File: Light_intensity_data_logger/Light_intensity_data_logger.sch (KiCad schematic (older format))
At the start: 15 parts

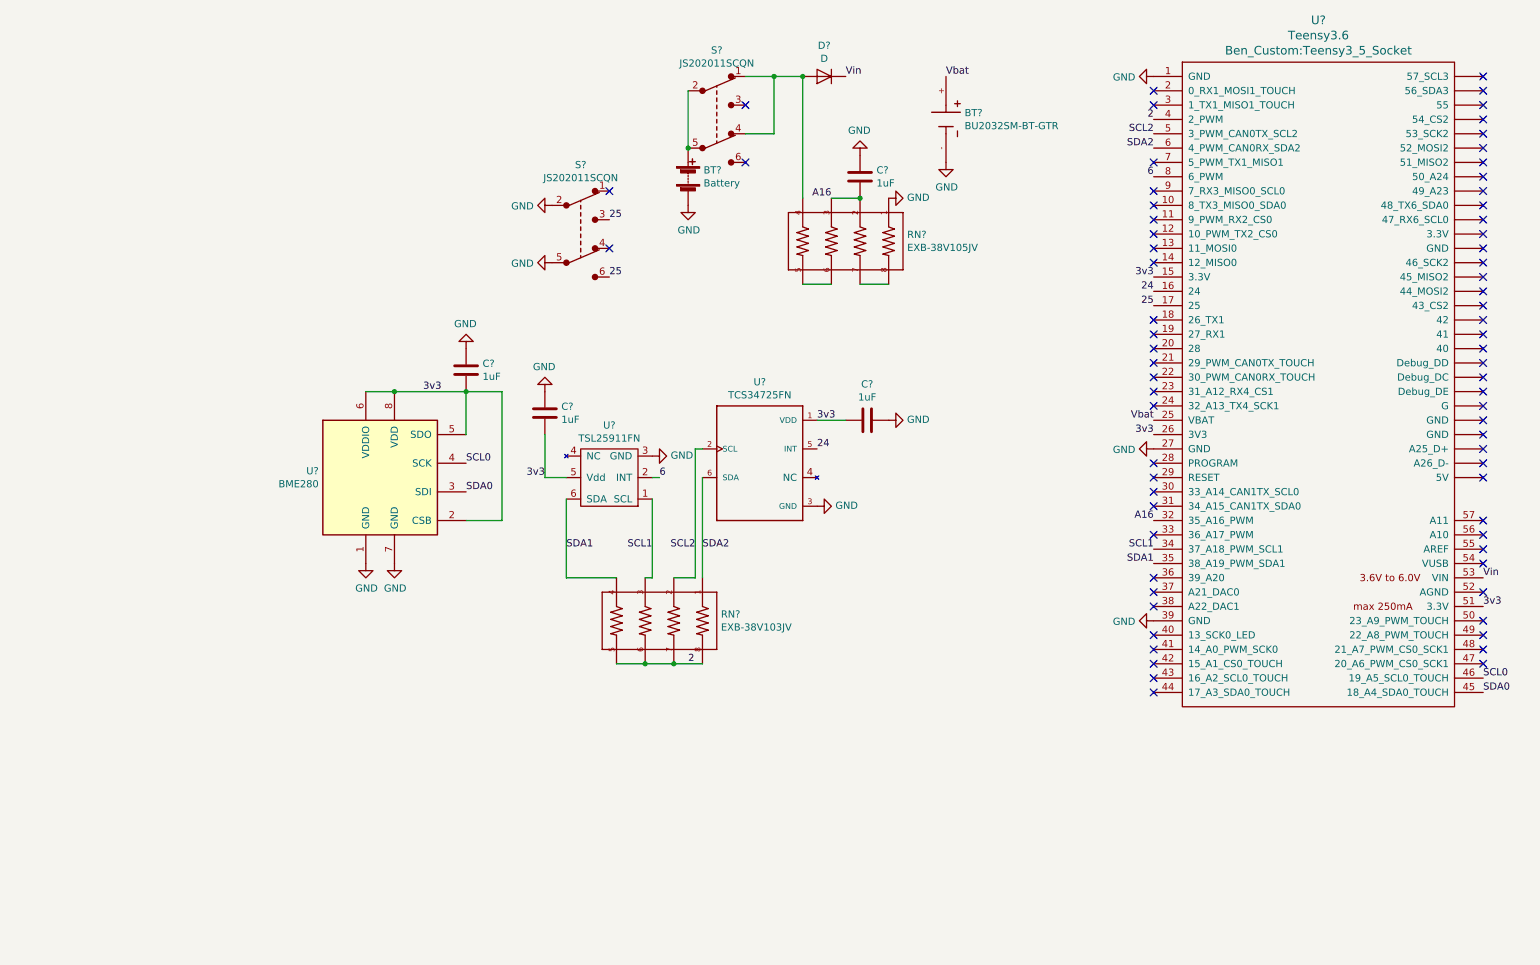
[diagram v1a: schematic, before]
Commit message: Add joystick and display
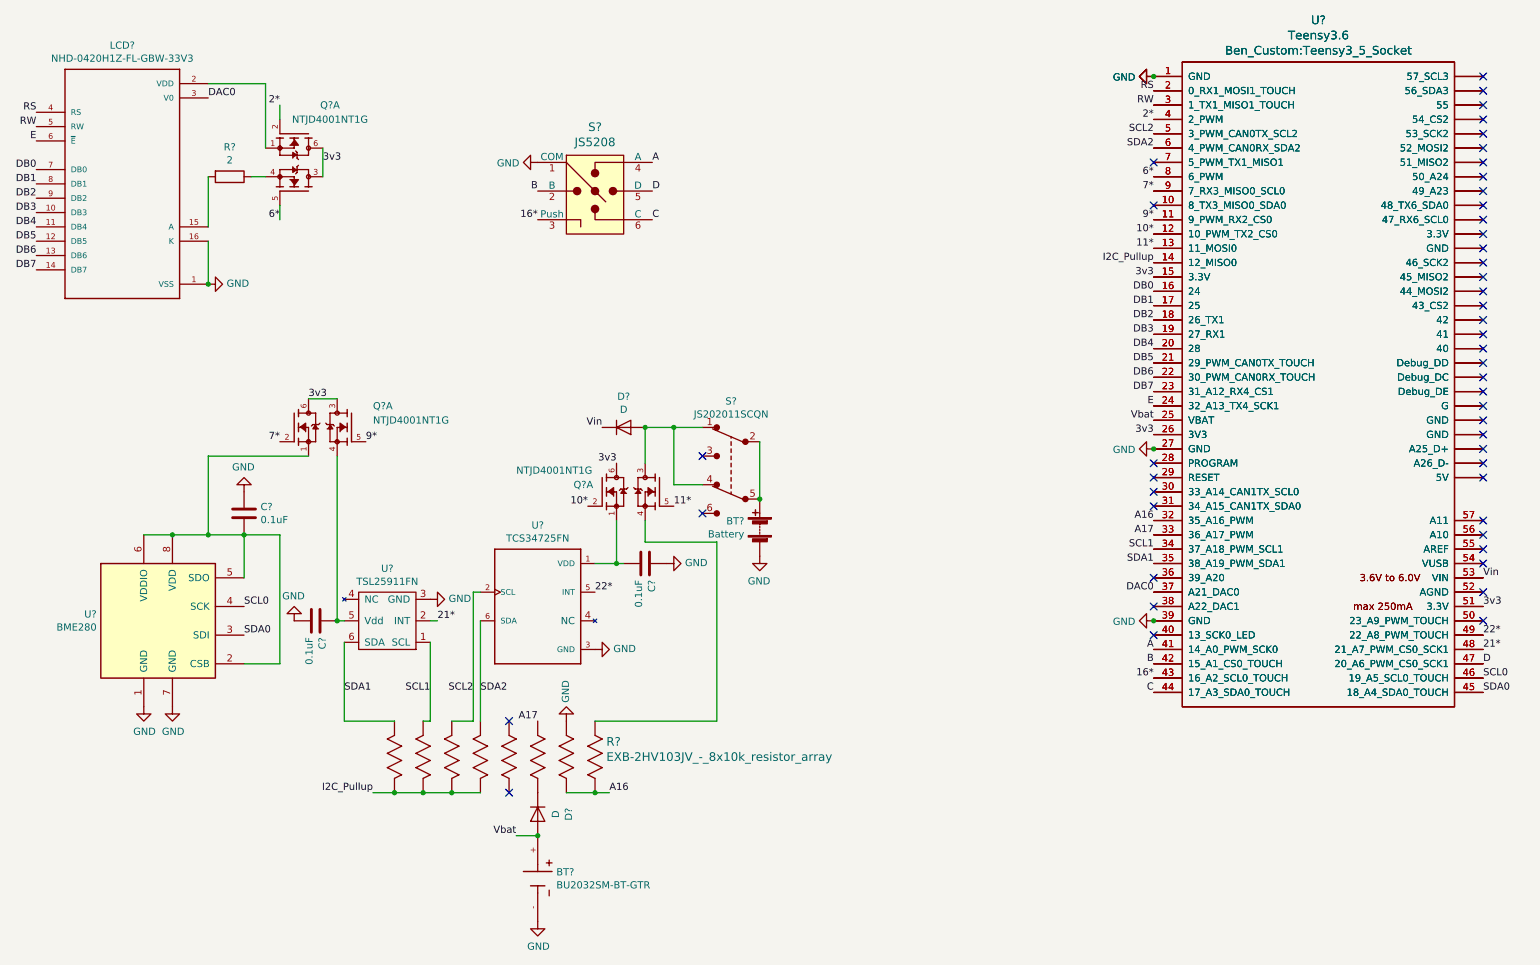
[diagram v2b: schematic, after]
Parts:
- removed C? (x3): 1uF, Capacitors_SMD:C_0603, symbol device:C
- removed RN?: EXB-38V103JV, RESCAXS80P320X160X60-8N, symbol Ben_custom:EXB-38V103JV
- removed RN?: EXB-38V105JV, RESCAXS80P320X160X60-8N, symbol Ben_custom:EXB-38V103JV
- removed S?: JS202011SCQN, digikey-footprints:Switch_Slide_JS202011SCQN, symbol dk_Slide-Switches:JS202011SCQN
- added C? (x2): 0.1uF, Capacitors_SMD:C_0603, symbol device:C
- added D?: D, Diodes_SMD:D_SOD-323, symbol device:D
- added LCD?: NHD-0420H1Z-FL-GBW-33V3, LCD_NHD-0420H1Z-FL-GBW-33V3, symbol Ben_custom:NHD-0420H1Z-FL-GBW-33V3
- added Q? (x3): NTJD4001NT1G, TO_SOT_Packages_SMD:SOT-363_SC-70-6, symbol Ben_custom:NTJD4001NT1G
- added R?: EXB-2HV103JV_-_8x10k_resistor_array, Ben_Custom:Resistor_array_1506_8x, symbol Ben_custom:EXB-2HV103JV_-_8x10k_resistor_array
- added R?: 2, Resistors_SMD:R_0603, symbol device:R
- added S?: JS5208, digikey-footprints:Switch_Nav_12.4x12.4mm_SMD_JS5208, symbol dk_Navigation-Switches-Joystick:JS5208
- added U?: Teensy3.6, Ben_Custom:Teensy3_5_Socket, symbol teensy:Teensy3.6
- C?: value 1uF -> 0.1uF; Part# 1276-6524-1-ND -> 311-1344-1-ND
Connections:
- net 3v3: now also Q?.3 (D2), Q?.3 (D2), Q?.6 (D1), Q?.6 (D1), Q?.6 (D1), U?.15 (3.3V), U?.26 (3V3), U?.51 (3.3V); no longer C?.2, U?.1 (VDD), U?.2 (CSB), U?.5 (SDO), U?.5 (Vdd), U?.6 (VDDIO), U?.8 (VDD)
- net A16: now also R?.15, R?.16, U?.32 (35_A16_PWM)
- net GND: now also C?.1, C?.2, LCD?.1 (VSS), LCD?.16 (K), R?.2, S?.1 (COM), U?.1 (GND), U?.27 (GND), U?.39 (GND)
- net SCL0: now also U?.46 (19_A5_SCL0_TOUCH)
- net SCL1: now also R?.7, U?.34 (37_A18_PWM_SCL1)
- net SCL2: now also R?.6, U?.5 (3_PWM_CAN0TX_SCL2)
- net SDA0: now also U?.45 (18_A4_SDA0_TOUCH)
- net SDA1: now also R?.8, U?.35 (38_A19_PWM_SDA1)
- net SDA2: now also R?.5, U?.6 (4_PWM_CAN0RX_SDA2)
- net Vbat: now also D?.2 (A), U?.25 (VBAT)
- net Vin: now also U?.53 (VIN)
- net at U?.10 (8_TX3_MISO0_SDA0): now also U?.10 (8_TX3_MISO0_SDA0)
- net 9*: now reaches U?.11 (9_PWM_RX2_CS0)
- net 9*: now also Q?.5 (G2), U?.11 (9_PWM_RX2_CS0)
- net 10*: now reaches U?.12 (10_PWM_TX2_CS0)
- net 10*: now also Q?.2 (G1), U?.12 (10_PWM_TX2_CS0)
- net 11*: now reaches U?.13 (11_MOSI0)
- net 11*: now also Q?.5 (G2), U?.13 (11_MOSI0)
- net I2C_Pullup: now reaches U?.14 (12_MISO0)
- net I2C_Pullup: now also R?.10, R?.11, R?.12, R?.9, U?.14 (12_MISO0)
- net DB2: now reaches U?.18 (26_TX1)
- net DB2: now also LCD?.9 (DB2), U?.18 (26_TX1)
- net DB3: now reaches U?.19 (27_RX1)
- net DB3: now also LCD?.10 (DB3), U?.19 (27_RX1)
- net RS: now reaches U?.2 (0_RX1_MOSI1_TOUCH)
- net RS: now also LCD?.4 (RS), U?.2 (0_RX1_MOSI1_TOUCH)
- net DB4: now reaches U?.20 (28)
- net DB4: now also LCD?.11 (DB4), U?.20 (28)
- net DB5: now reaches U?.21 (29_PWM_CAN0TX_TOUCH)
- net DB5: now also LCD?.12 (DB5), U?.21 (29_PWM_CAN0TX_TOUCH)
- net DB6: now reaches U?.22 (30_PWM_CAN0RX_TOUCH)
- net DB6: now also LCD?.13 (DB6), U?.22 (30_PWM_CAN0RX_TOUCH)
- net DB7: now reaches U?.23 (31_A12_RX4_CS1)
- net DB7: now also LCD?.14 (DB7), U?.23 (31_A12_RX4_CS1)
- net E: now reaches U?.24 (32_A13_TX4_SCK1)
- net E: now also LCD?.6 (~E~), U?.24 (32_A13_TX4_SCK1)
- net at U?.28 (PROGRAM): now also U?.28 (PROGRAM)
- net at U?.29 (RESET): now also U?.29 (RESET)
- net RW: now reaches U?.3 (1_TX1_MISO1_TOUCH)
- net RW: now also LCD?.5 (RW), U?.3 (1_TX1_MISO1_TOUCH)
- net at U?.30 (33_A14_CAN1TX_SCL0): now also U?.30 (33_A14_CAN1TX_SCL0)
- net at U?.31 (34_A15_CAN1TX_SDA0): now also U?.31 (34_A15_CAN1TX_SDA0)
- net A17: now reaches U?.33 (36_A17_PWM)
- net A17: now also R?.3, U?.33 (36_A17_PWM)
- net at U?.36 (39_A20): now also U?.36 (39_A20)
- net DAC0: now reaches U?.37 (A21_DAC0)
- net DAC0: now also LCD?.3 (V0), U?.37 (A21_DAC0)
- net at U?.38 (A22_DAC1): now also U?.38 (A22_DAC1)
- net at U?.40 (13_SCK0_LED): now also U?.40 (13_SCK0_LED)
- net A: now reaches U?.41 (14_A0_PWM_SCK0)
- net A: now also S?.4 (A), U?.41 (14_A0_PWM_SCK0)
- net B: now reaches U?.42 (15_A1_CS0_TOUCH)
- net B: now also S?.2 (B), U?.42 (15_A1_CS0_TOUCH)
- net 16*: now reaches U?.43 (16_A2_SCL0_TOUCH)
- net 16*: now also S?.3 (Push), U?.43 (16_A2_SCL0_TOUCH)
- net C: now reaches U?.44 (17_A3_SDA0_TOUCH)
- net C: now also S?.6 (C), U?.44 (17_A3_SDA0_TOUCH)
- net D: now reaches U?.47 (20_A6_PWM_CS0_SCK1)
- net D: now also S?.5 (D), U?.47 (20_A6_PWM_CS0_SCK1)
- net 21*: now reaches U?.48 (21_A7_PWM_CS0_SCK1)
- net 21*: now also U?.2 (INT), U?.48 (21_A7_PWM_CS0_SCK1)
- net 22*: now reaches U?.49 (22_A8_PWM_TOUCH)
- net 22*: now also U?.5 (INT), U?.49 (22_A8_PWM_TOUCH)
- net at U?.50 (23_A9_PWM_TOUCH): now also U?.50 (23_A9_PWM_TOUCH)
- net at U?.52 (AGND): now also U?.52 (AGND)
- net at U?.54 (VUSB): now also U?.54 (VUSB)
- net at U?.55 (AREF): now also U?.55 (AREF)
- net at U?.56 (A10): now also U?.56 (A10)
- net at U?.57 (A11): now also U?.57 (A11)
- net at U?.7 (5_PWM_TX1_MISO1): now also U?.7 (5_PWM_TX1_MISO1)
- net 7*: now reaches U?.9 (7_RX3_MISO0_SCL0)
- net 7*: now also Q?.2 (G1), U?.9 (7_RX3_MISO0_SCL0)
- net at U?.~ (GND): now also U?.~ (GND)
- net at D?.2 (A), S?.1, S?.4: now also Q?.3 (D2)
- net 2 renamed 2*
- net 2*: now also Q?.2 (G1), U?.4 (2_PWM)
- net 24 renamed DB0
- net DB0: now also LCD?.7 (DB0), U?.16 (24); no longer U?.5 (INT)
- net 25 renamed DB1
- net DB1: now also LCD?.8 (DB1), U?.17 (25)
- net 6 renamed 6*
- net 6*: now also Q?.5 (G2), U?.8 (6_PWM); no longer U?.2 (INT)
- new net: U?.~ (GND), U?.~ (GND) (x28)
- new net: C?.2, Q?.1 (S1), U?.1 (VDD)
- new net: C?.1, Q?.4 (S2), U?.5 (Vdd)
- new net: C?.2, Q?.1 (S1), U?.2 (CSB), U?.5 (SDO), U?.6 (VDDIO), U?.8 (VDD)
- new net: LCD?.15 (A), R?.2
- new net: LCD?.2 (VDD), Q?.1 (S1)
- new net: Q?.4 (S2), R?.1 (x2)
- new net: D?.1 (K), R?.14
- no-connect marks 71 -> 48
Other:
- moved on the sheet: BT?, C?, D?, S?, U?

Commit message: Add claw headers and initial PCB layout
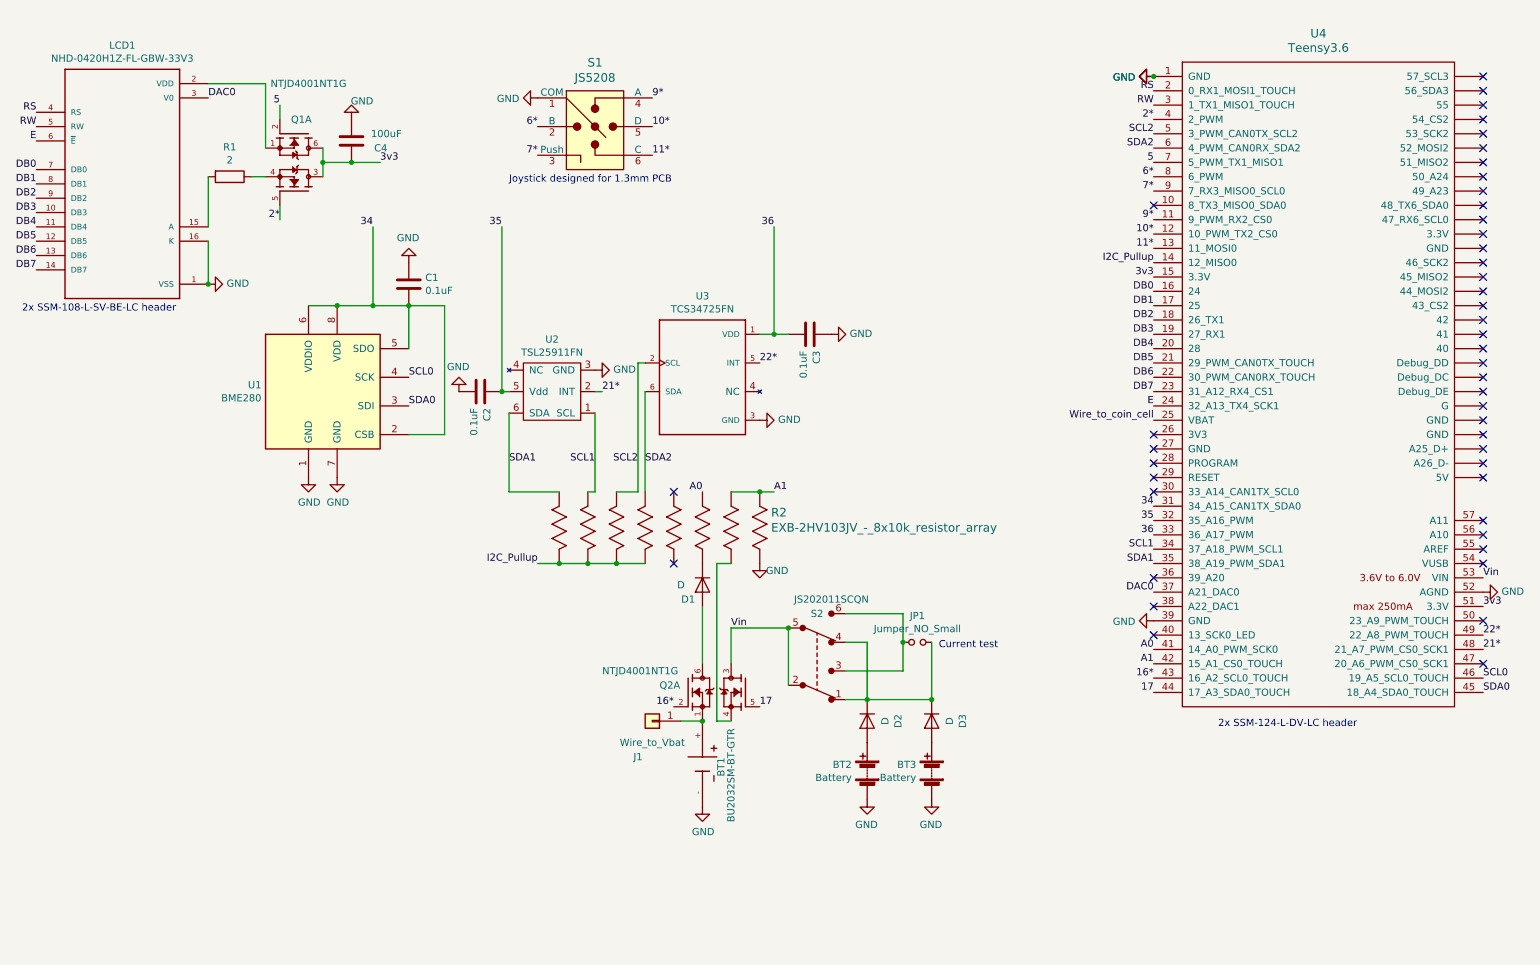
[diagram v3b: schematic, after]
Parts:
- removed Q?: NTJD4001NT1G, TO_SOT_Packages_SMD:SOT-363_SC-70-6, symbol Ben_custom:NTJD4001NT1G
- removed U?: Teensy3.6, Ben_Custom:Teensy3_5_Socket, symbol teensy:Teensy3.6
- added BT3: Battery, Ben_Custom:BH3AAW-Battery_wire_pads, symbol device:Battery
- added C4: 100uF, Capacitors_SMD:C_1206, symbol device:C
- added D3: D, Diodes_SMD:D_SOD-323, symbol device:D
- added J1: Wire_to_Vbat, Wire_Pads:SolderWirePad_single_SMD_5x10mm, symbol conn:Conn_01x01
- added JP1: Jumper_NO_Small, Ben_Custom:Banana_Jack_2Pin, symbol device:Jumper_NO_Small
- BT2: renamed from BT?; Part# BH3AA-W-ND -> SBH331A-ND
- LCD1: renamed from LCD?; footprint LCD_NHD-0420H1Z-FL-GBW-33V3 -> Ben_Custom:NHD-0420H1Z-FL-GBW-33V3_Display_with_Header; Field4 IPC-7351B -> (none); Field5 Newheaven Display -> (none); Field6 02 -> (none); Part# (none) -> NHD-0420H1Z-FL-GBW-33V3
- U1: renamed from U?; footprint Housings_LGA:LGA-8_2.5x2.5mm_Pitch0.65mm -> digikey-footprints:Pressure_Sensor_LGA-8_2.5x2.5mm_BME280
- U4: renamed from U?; footprint Ben_Custom:Teensy3_5_Socket -> Ben_Custom:Teensy3.6_doublewide_header; Part# (none) -> 1568-1465-ND
- gave numbers to parts that had none: 14
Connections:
- net 10*: now also S1.5 (D); no longer Q2.2 (G1)
- net 11*: now also S1.6 (C); no longer Q2.5 (G2)
- net 16*: now also Q2.2 (G1); no longer S1.3 (Push)
- net 2*: now also Q1.5 (G2); no longer Q1.2 (G1)
- net 3v3: now also C4.1; no longer Q2.6 (D1), U4.26 (3V3)
- net 6*: now also S1.2 (B); no longer Q1.5 (G2)
- net 7*: now also S1.3 (Push)
- net 9*: now also S1.4 (A)
- net GND: now also R2.16, U4.52 (AGND), BT3.2 (-), C4.2; no longer R2.2, U4.27 (GND)
- net Vin: now also Q2.3 (D2), S2.2, S2.5; no longer D2.1 (K)
- net 34: now reaches U4.31 (34_A15_CAN1TX_SDA0)
- net 34: now also C1.2, U1.2 (CSB), U1.5 (SDO), U1.6 (VDDIO), U1.8 (VDD)
- net 5: now reaches U4.7 (5_PWM_TX1_MISO1)
- net 5: now also Q1.2 (G1)
- net 36: now reaches C3.2, U3.1 (VDD)
- net 36: now also U4.33 (36_A17_PWM); no longer Q2.1 (S1)
- net 35: now reaches C2.1, U2.5 (Vdd)
- net 35: now also U4.32 (35_A16_PWM)
- net at S2.1, S2.4: now also D2.1 (K), D3.1 (K), JP1.2; no longer D2.2 (A), Q2.3 (D2)
- net at S2.3: now also S2.6, JP1.1
- net at Q2.4 (S2): now also R2.15; no longer R2.1
- net A renamed A0
- net A0: now also R2.3; no longer S1.4 (A)
- removed net A16: R2.15, R2.16, U4.32 (35_A16_PWM)
- removed net A17: R2.3, U4.33 (36_A17_PWM)
- net B renamed A1
- net A1: now also R2.1, R2.2; no longer S1.2 (B)
- net C renamed 17
- net 17: now also Q2.5 (G2); no longer S1.6 (C)
- net D: no longer names the net of U4.47 (20_A6_PWM_CS0_SCK1)
- net D: no longer S1.5 (D)
- removed net Vbat: BT1.+, D1.2 (A), U4.25 (VBAT)
- new net: BT2.1 (+), D2.2 (A)
- new net: BT1.+, J1.1 (Pin_1), Q2.1 (S1)
- new net: BT3.1 (+), D3.2 (A)
- new net: D1.2 (A), Q2.6 (D1)
- new net Wire_to_coin_cell: U4.25 (VBAT)
- now unconnected: U4.~ (GND), U4.~ (GND), U4.~ (GND), U4.~ (GND), U4.~ (GND), U4.~ (GND), U4.~ (GND), U4.~ (GND), U4.~ (GND), U4.~ (GND), U4.~ (GND), U4.~ (GND), U4.~ (GND), U4.~ (GND), U4.~ (GND), U4.~ (GND), U4.~ (GND), U4.~ (GND), U4.~ (GND), U4.~ (GND), U4.~ (GND), U4.~ (GND), U4.~ (GND), U4.~ (GND), U4.~ (GND), U4.~ (GND), U4.~ (GND), U4.~ (GND)
- no-connect marks 48 -> 46
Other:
- note added: "2x SSM-108-L-SV-BE-LC header"
- note added: "2x SSM-124-L-DV-LC header"
- note added: "Current test"
- note added: "Joystick designed for 1.3mm PCB"
- moved on the sheet: BT1, BT2, C1, C2, C3, D1, D2, Q2A, R2, S1, S2, U1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
